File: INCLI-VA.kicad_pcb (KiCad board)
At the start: 2 copper layers, 100 x 100 mm, 167 parts, among them J1 MSTBV 2,5/5-GF-5,08, J2 MSTBV 2,5/2-GF-5,08, J401 USB4105-GF-A, J402 UART0, Q101 STD18NF25, Q102 IPD30N10S3L-34, Q701 DMN10H220LQ, Q751 DMN10H220LQ, SW401 RESET, SW402 BOOT, U101 LM74930QRGERQ1, U201 LMR38010SQDDARQ1, U301 TPS62A02QDRLRQ1, U302 LP5907QMFX-3.3Q1, U401 ESP32-S3-WROOM-1-N8R2, U402 USBLC6-2SC6, U501 SCL3300-D01, U502 ASM330LHHTR, U503 AS5147U-HTSM, U601 ADM3055E, U701 74AHCT1G126, U751 74AHCT1G126, U801 TPS3828-33Q1

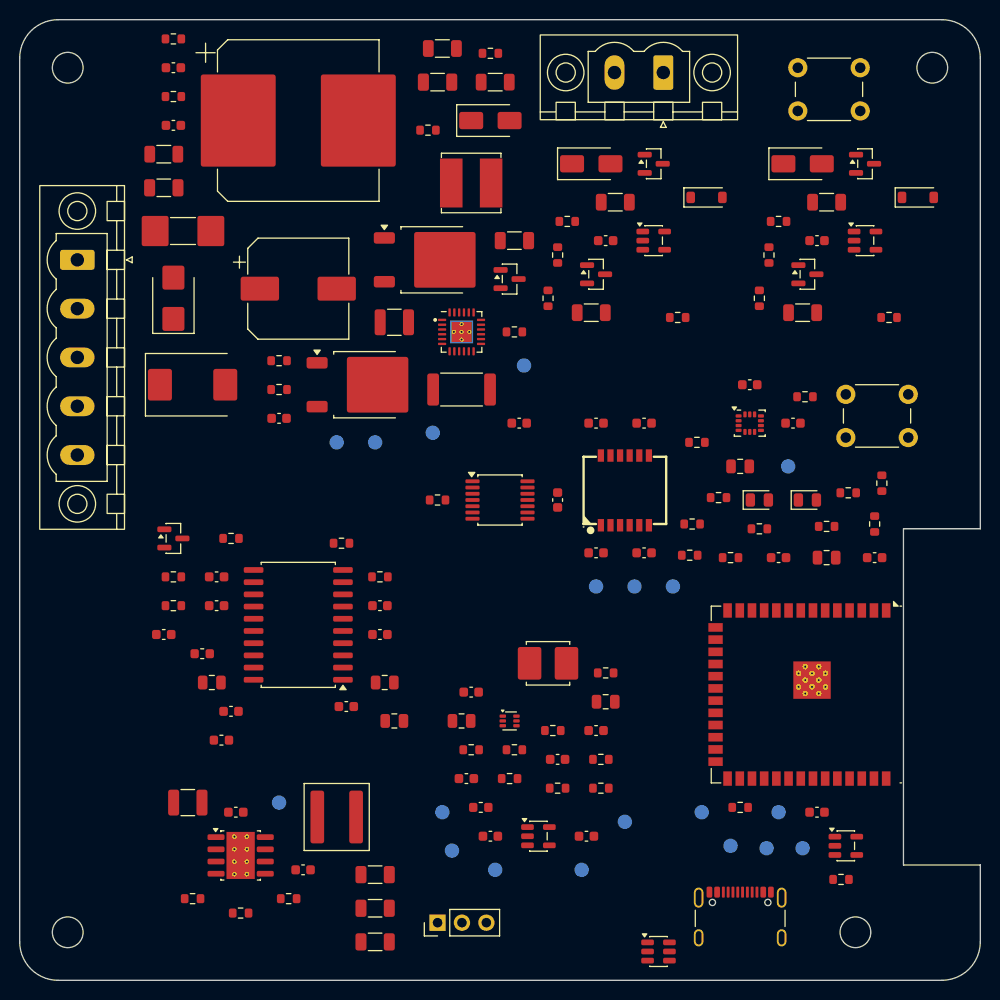
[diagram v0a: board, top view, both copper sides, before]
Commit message: [Claude Code] PCB: reacomodo por bloques segun docs/reference, H5 intermedio y barrera CAN
- Entrada -> proteccion -> bulk -> buck en la esquina superior izquierda;
  pasivos de U101 junto a sus pines; C107/C106 junto a la salida de L101.
- CAN: U601 sobre la barrera con el lado aislado hacia J1; rule area
  BARRERA_CAN en F.Cu/B.Cu (solo U601 la cruza; FB602 es aislado-aislado).
  DRU: pin 17 de U601 (AUXOUT NC) cuenta como dominio aislado.
- DO1/DO2 bajo su pin de J2 (antes cruzados). USB-C al borde derecho con
  U402 en linea; SW401 junto al EN; C402/C401 en los pines de 3V3.
- H5 (M3 NPTH) en esquematico y PCB junto a U501/U502, a 18 mm del eje ROT.
- DRC 0 errores / 1 aviso U401 / paridad 0; ERC 0 / 1 aviso conocido.
- Incluye docs/reference (fotos UG-230 e INCLIMAX) y scripts/layout_bloques.

Co-Authored-By: Claude Opus 5.5 <noreply@anthropic.com>
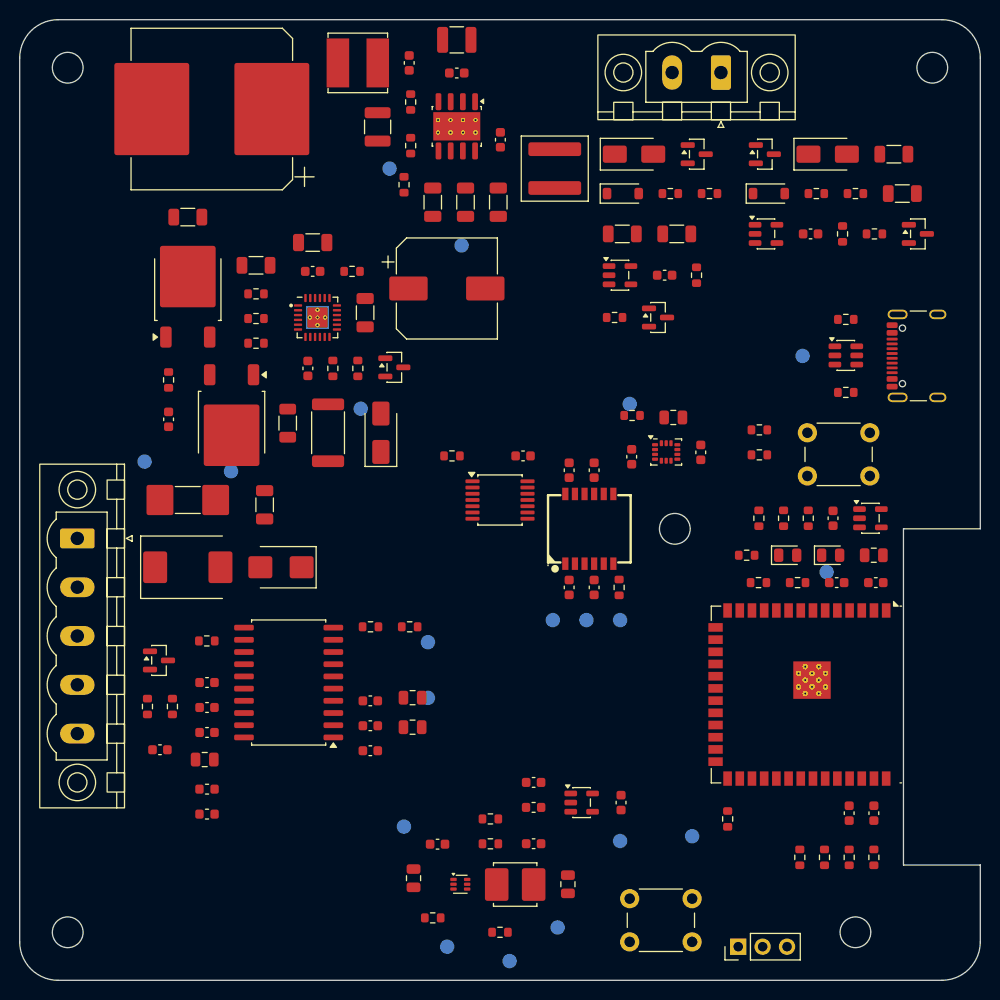
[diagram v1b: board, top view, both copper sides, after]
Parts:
- added H5: MountingHole_M3, MountingHole:MountingHole_3.2mm_M3, F.Cu at (168.2, 103.0)
- moved R203 86.0 mm to (140.7, 58.6), turned to 90 degrees
- moved C201 84.2 mm to (145.5, 52.1)
- moved C202 80.3 mm to (145.5, 55.5), turned to 180 degrees
- moved R201 79.4 mm to (140.7, 63.1), turned to 90 degrees
- moved U201 79.2 mm to (145.5, 61.1), turned to -90 degrees
- moved C203 78.7 mm to (150.0, 62.5), turned to 90 degrees
- moved C206 78.1 mm to (149.8, 69.0), turned to 90 degrees
- moved R202 77.7 mm to (140.0, 67.2), turned to 90 degrees
- moved C205 74.1 mm to (146.4, 69.0), turned to 90 degrees
- moved L201 71.2 mm to (155.7, 65.5), turned to -90 degrees
- moved C204 70.3 mm to (143.0, 69.0), turned to 90 degrees
- moved U402 65.0 mm to (186.0, 85.0)
- moved J401 62.6 mm to (194.5, 85.0), turned to 90 degrees
- moved TP201 61.0 mm to (146.0, 73.5)
- moved SW402 57.1 mm to (163.5, 141.5)
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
